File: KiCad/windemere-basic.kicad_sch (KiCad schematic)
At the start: 56 parts, among them J1 Barrel_Jack, J2 Connector, SW1 SW_SPDT, SW2 Push_Button, U1 L7805, U2 74HC00, U3 WD65C02, U4 28C256, U5 62256, U6 WD65C22, U7 MM74C922, U8 HD44780U, U9 MCP102-475, X1 1MHz

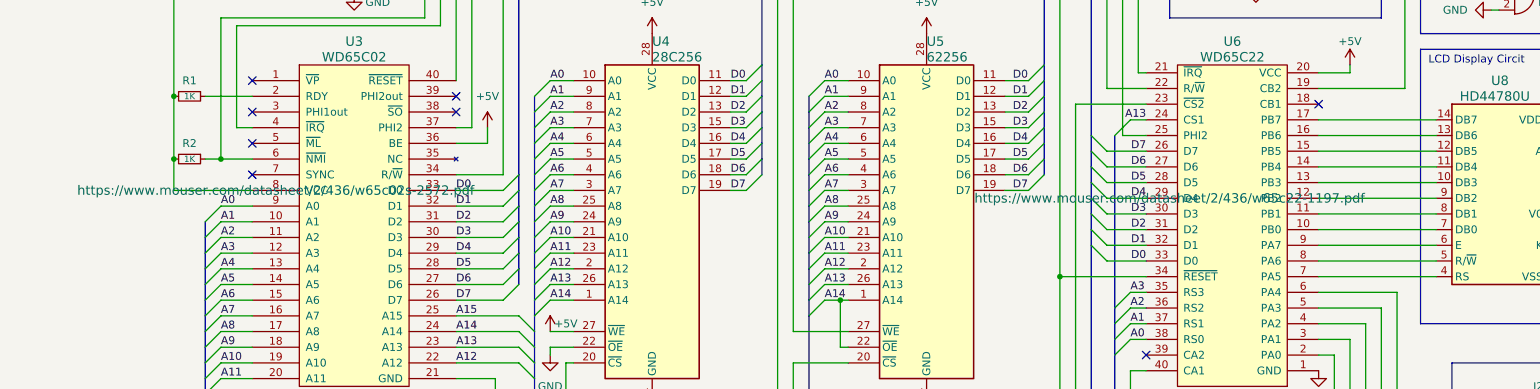
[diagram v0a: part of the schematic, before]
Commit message: Add Zif socket to eprom
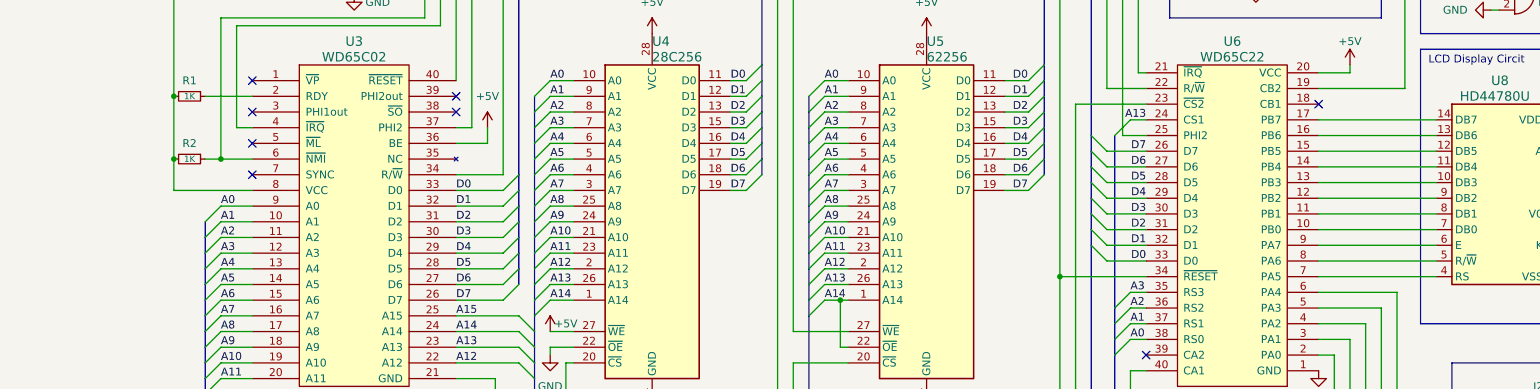
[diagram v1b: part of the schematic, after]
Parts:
- X1: Mouser Part (none) -> 520-TCF100-X
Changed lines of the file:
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@@
     )
     (property "Datasheet" "https://www.mouser.com/datasheet/2/436/w65c02s-2572.pdf" (id 3) (at 34.29 66.04 0)
-      (effects (font (size 1.524 1.524)))
+      (effects (font (size 1.524 1.524)) hide)
     )
     (property "Digikey Part" "~" (id 4) (at 46.99 71.12 0)
@@
       (effects (font (size 1.27 1.27)) hide)
     )
+    (property "Mouser Part" "520-TCF100-X" (id 5) (at 46.99 26.67 0)
+      (effects (font (size 1.27 1.27)) hide)
+    )
     (pin "1")
     (pin "14")
@@
     )
     (property "Datasheet" "https://www.mouser.com/datasheet/2/436/w65c22-1197.pdf" (id 3) (at 179.07 67.31 0)
-      (effects (font (size 1.524 1.524)))
+      (effects (font (size 1.524 1.524)) hide)
     )
     (property "Digikey Part" "~" (id 4) (at 189.23 72.39 0)

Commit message: update socket
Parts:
- SW2: value Push_Button -> Reset Button
- U4: footprint Package_DIP:DIP-28_W15.24mm -> sockets:eeprom_socket
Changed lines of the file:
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@@
       (effects (font (size 1.27 1.27)) (justify right))
     )
-    (property "Value" "Push_Button" (id 1) (at 186.69 31.7499 90)
+    (property "Value" "Reset Button" (id 1) (at 186.69 31.7499 90)
       (effects (font (size 1.27 1.27)) (justify right) hide)
     )
@@
       (effects (font (size 1.524 1.524)) (justify left))
     )
-    (property "Footprint" "Package_DIP:DIP-28_W15.24mm" (id 2) (at 95.25 71.12 0)
+    (property "Footprint" "sockets:eeprom_socket" (id 2) (at 95.25 71.12 0)
       (effects (font (size 1.27 1.27)) hide)
     )
@@
     )
     (path "/cee2649a-819a-40cb-8cce-25f9ff3a4017"
-      (reference "SW2") (unit 1) (value "Push_Button") (footprint "footprints:D6R90F1LFS")
+      (reference "SW2") (unit 1) (value "Reset Button") (footprint "footprints:D6R90F1LFS")
     )
     (path "/af950b64-290c-45ec-af5b-2091c768d43e"
@@
     )
     (path "/d218171f-2b8a-4061-9bea-fd463a7d5174"
-      (reference "U4") (unit 1) (value "28C256") (footprint "Package_DIP:DIP-28_W15.24mm")
+      (reference "U4") (unit 1) (value "28C256") (footprint "sockets:eeprom_socket")
     )
     (path "/40f344b6-38d5-4cfc-82df-1f570acc5b8b"

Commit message: update to current
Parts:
- removed SW1: SW_SPDT, Button_Switch_THT:SW_E-Switch_EG1271_DPDT, symbol Switch:SW_SPDT
- SW2: value Reset Button -> (none); footprint footprints:D6R90F1LFS -> (none)
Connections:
- net at D1.2 (A): now also J1.1
- no-connect marks 10 -> 9
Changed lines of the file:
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@@
   (no_connect (at 30.48 63.5))
   (no_connect (at 30.48 53.34))
-  (no_connect (at 22.86 143.51))
   (no_connect (at 175.26 92.71))
   (no_connect (at 63.5 50.8))
@@
     (stroke (width 0) (type default) (color 0 0 0 0))
   )
-  (wire (pts (xy 22.86 138.43) (xy 19.05 138.43))
-    (stroke (width 0) (type default) (color 0 0 0 0))
-  )
   (bus (pts (xy 226.06 142.24) (xy 226.06 144.78))
     (stroke (width 0) (type default) (color 0 0 0 0))
@@
     (stroke (width 0) (type default) (color 0 0 0 0))
   )
-  (wire (pts (xy 19.05 138.43) (xy 19.05 161.29))
+  (wire (pts (xy 19.05 140.97) (xy 19.05 161.29))
     (stroke (width 0) (type default) (color 0 0 0 0))
   )
@@
     (stroke (width 0) (type default) (color 0 0 0 0))
   )
-  (wire (pts (xy 33.02 140.97) (xy 36.83 140.97))
+  (wire (pts (xy 19.05 140.97) (xy 36.83 140.97))
     (stroke (width 0) (type default) (color 0 0 0 0))
   )
@@
     (effects (font (size 1.27 1.27)) (justify left bottom))
   )
-  (symbol (lib_id "Switch:SW_SPDT") (at 27.94 140.97 0) (mirror y) (unit 1)
-    (in_bom yes) (on_board yes)
-    (property "Reference" "SW1" (id 0) (at 27.94 133.731 0))
-    (property "Value" "SW_SPDT" (id 1) (at 27.94 136.0424 0))
-    (property "Footprint" "Button_Switch_THT:SW_E-Switch_EG1271_DPDT" (id 2) (at 27.94 140.97 0)
-      (effects (font (size 1.27 1.27)) hide)
-    )
-    (property "Datasheet" "~" (id 3) (at 27.94 140.97 0)
-      (effects (font (size 1.27 1.27)) hide)
-    )
-    (pin "1")
-    (pin "2")
-    (pin "3")
-  )
   (symbol (lib_id "power:GND") (at 46.99 34.29 0) (unit 1)
     (in_bom yes) (on_board yes)
@@
       (effects (font (size 1.27 1.27)) hide)
     )
+    (pin "1")
+    (pin "2")
+    (pin "3")
     (pin "4")
     (pin "5")
     (pin "6")
+    (pin "10")
+    (pin "8")
+    (pin "9")
+    (pin "11")
+    (pin "12")
+    (pin "13")
+    (pin "14")
+    (pin "7")
   )
   (symbol (lib_id "power:GND") (at 231.14 36.83 270) (mirror x) (unit 1)
@@
       (effects (font (size 1.27 1.27)) hide)
     )
+    (pin "1")
+    (pin "2")
+    (pin "3")
+    (pin "4")
+    (pin "5")
+    (pin "6")
+    (pin "10")
+    (pin "8")
+    (pin "9")
+    (pin "11")
+    (pin "12")
+    (pin "13")
     (pin "14")
     (pin "7")
@@
       (effects (font (size 1.27 1.27)) hide)
     )
+    (pin "1")
+    (pin "2")
+    (pin "3")
+    (pin "4")
+    (pin "5")
+    (pin "6")
     (pin "10")
     (pin "8")
     (pin "9")
+    (pin "11")
+    (pin "12")
+    (pin "13")
+    (pin "14")
+    (pin "7")
   )
   (symbol (lib_id "Switch:SW_Push_45deg") (at 114.3 171.45 90) (unit 1)
@@
     (pin "2")
     (pin "3")
+    (pin "4")
+    (pin "5")
+    (pin "6")
+    (pin "10")
+    (pin "8")
+    (pin "9")
+    (pin "11")
+    (pin "12")
+    (pin "13")
+    (pin "14")
+    (pin "7")
   )
   (symbol (lib_id "power:GND") (at 231.14 104.14 270) (unit 1)
@@
       (effects (font (size 1.27 1.27)) (justify right))
     )
-    (property "Value" "Reset Button" (id 1) (at 186.69 31.7499 90)
+    (property "Value" "" (id 1) (at 186.69 31.7499 90)
       (effects (font (size 1.27 1.27)) (justify right) hide)
     )
-    (property "Footprint" "footprints:D6R90F1LFS" (id 2) (at 187.96 30.48 0)
+    (property "Footprint" "" (id 2) (at 187.96 30.48 0)
       (effects (font (size 1.27 1.27)) hide)
     )
@@
       (reference "RV1") (unit 1) (value "10K") (footprint "Potentiometer_THT:Potentiometer_Bourns_3296W_Vertical")
     )
-    (path "/0086ff9a-4369-44c7-b877-26a7c9394b1d"
-      (reference "SW1") (unit 1) (value "SW_SPDT") (footprint "Button_Switch_THT:SW_E-Switch_EG1271_DPDT")
-    )
     (path "/cee2649a-819a-40cb-8cce-25f9ff3a4017"
-      (reference "SW2") (unit 1) (value "Reset Button") (footprint "footprints:D6R90F1LFS")
+      (reference "SW2") (unit 1) (value "Reset Button") (footprint "Button_Switch_THT:SW_PUSH_6mm")
     )
     (path "/af950b64-290c-45ec-af5b-2091c768d43e"

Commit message: Update ID's
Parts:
- SW1: renamed from SW2; value (none) -> Reset Button; footprint (none) -> Button_Switch_THT:SW_PUSH_6mm
- renumbered C4 to C1, C3 to C2, C5 to C3, C6 to C4, C1 to C5, C2 to C6, D2 to D1, D1 to D2, J2 to J1, J1 to J2, KB18 to KB10, KB3 to KB11, KB7 to KB12, KB11 to KB13, KB15 to KB14, KB19 to KB15, KB4 to KB16, KB8 to KB17, KB12 to KB18, KB16 to KB19, KB5 to KB2, KB9 to KB3, KB13 to KB4, KB17 to KB5, KB2 to KB6, KB6 to KB7, KB10 to KB8, KB14 to KB9, R8 to R1, R1 to R2, R2 to R3, R3 to R4, R4 to R5, R5 to R6, R6 to R7, R7 to R8, U8 to U1, U3 to U2, U4 to U3, U5 to U4, U6 to U5, U2 to U6, U1 to U8

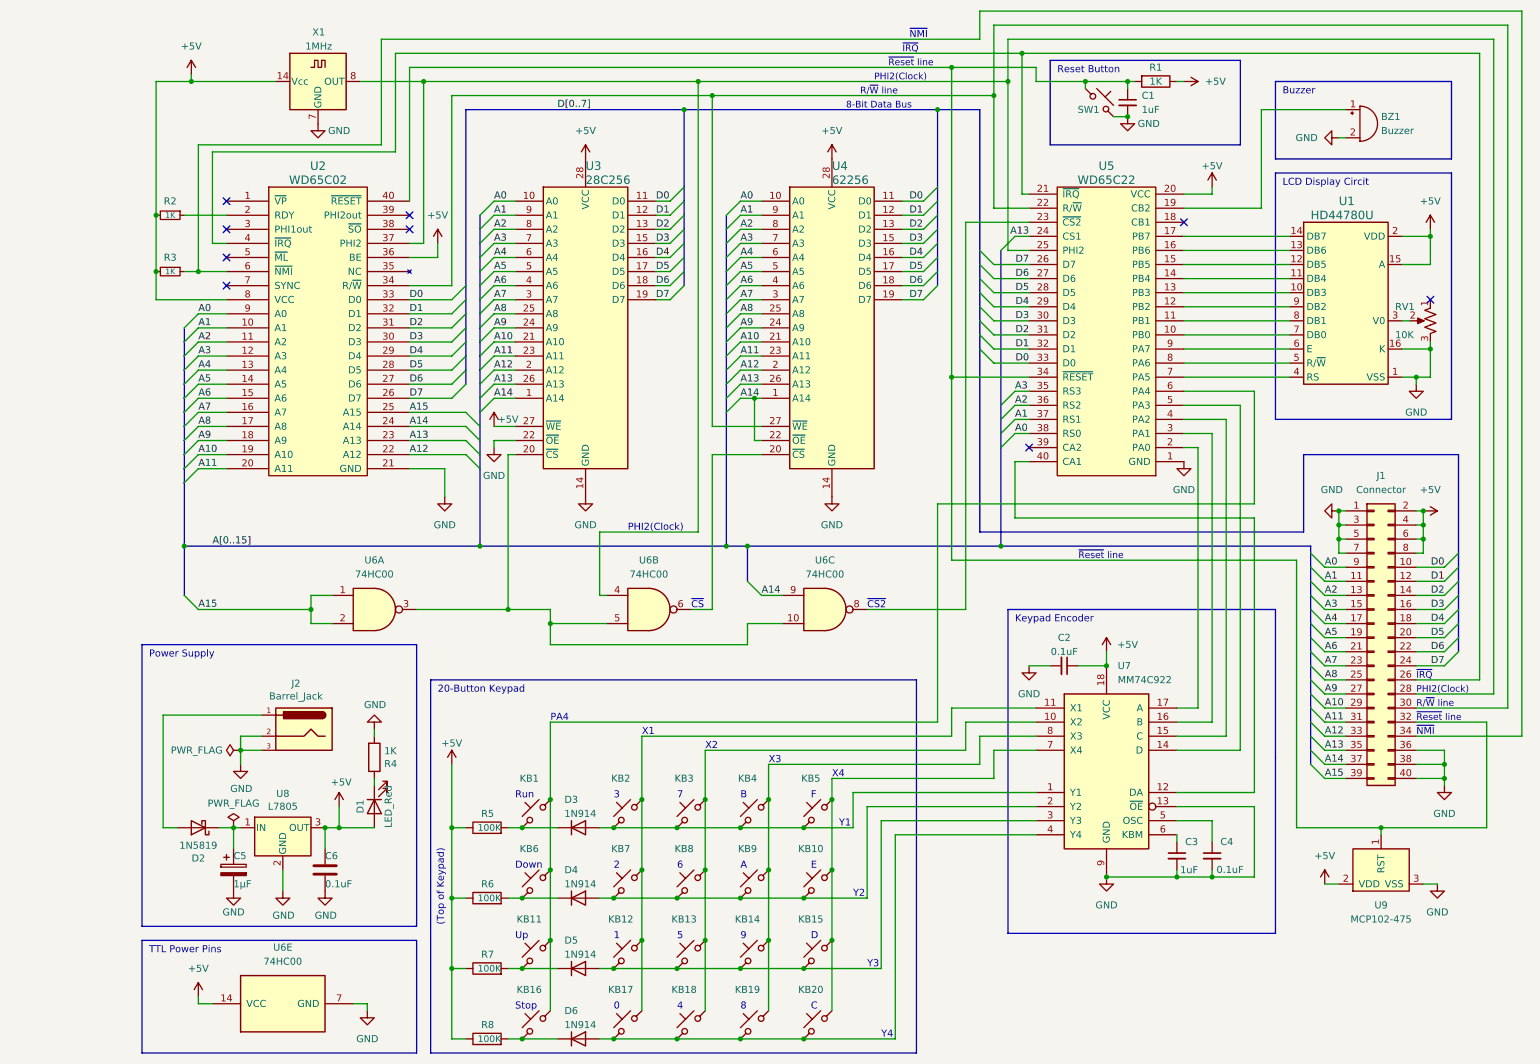
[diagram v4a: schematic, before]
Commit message: Add Bypass caps
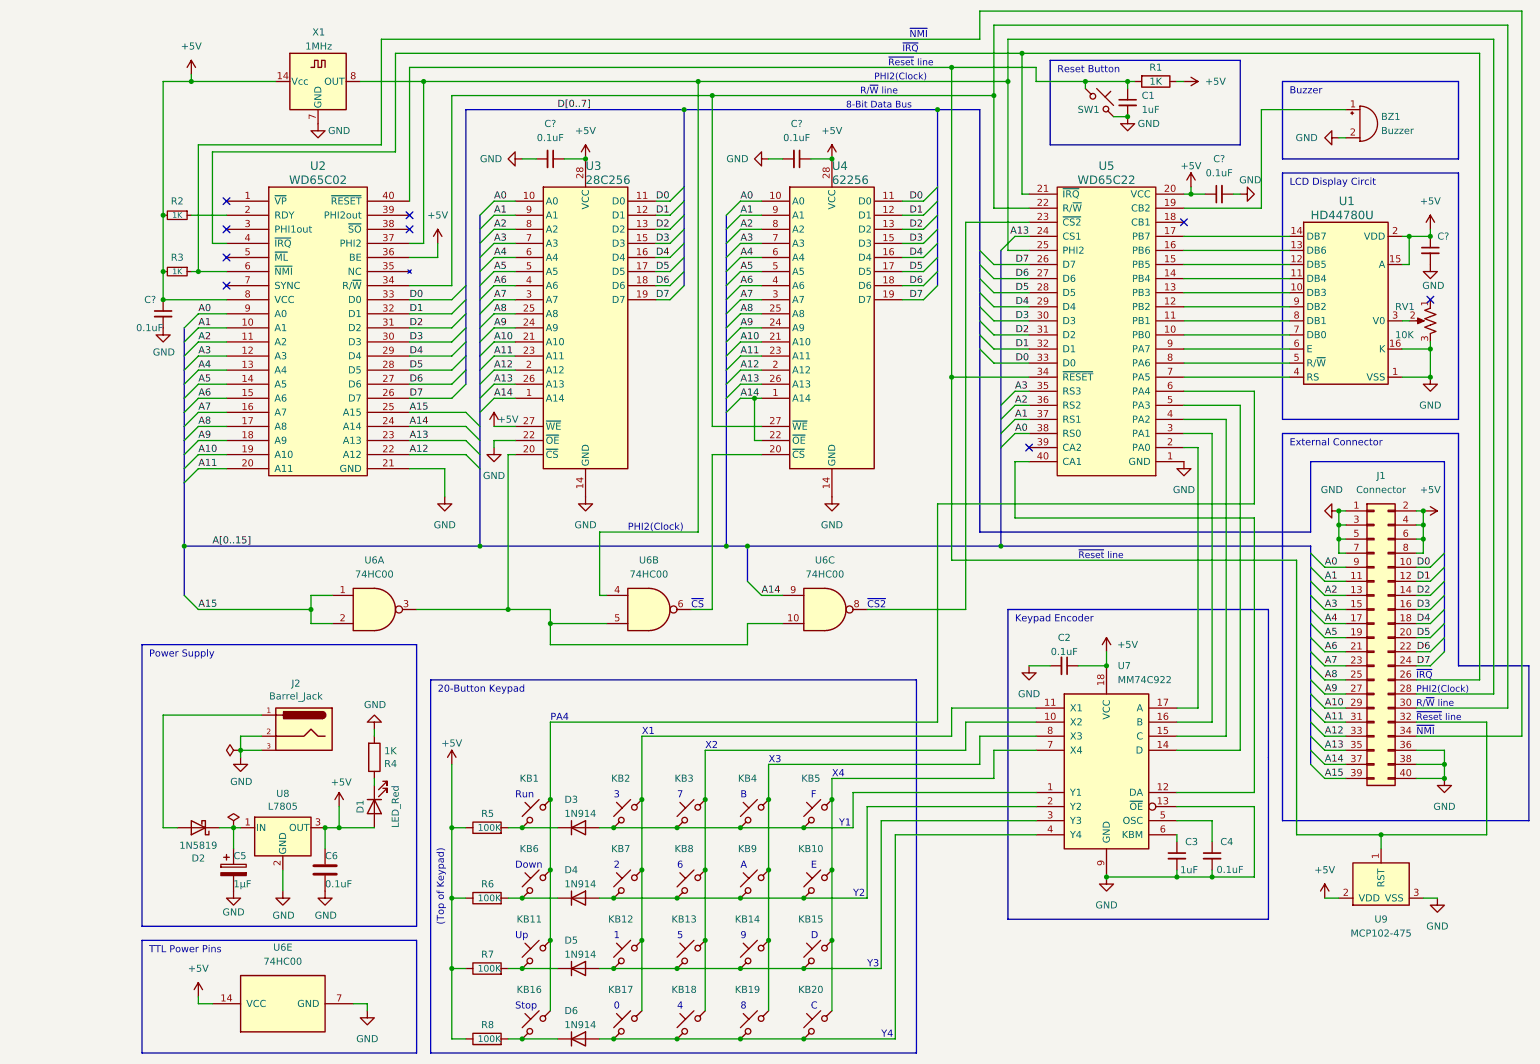
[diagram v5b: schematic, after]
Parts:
- added C? (x4): 0.1uF, Capacitor_THT:C_Disc_D7.0mm_W2.5mm_P5.00mm, symbol Device:C_Small
- added C?: (no value), Capacitor_THT:C_Disc_D7.0mm_W2.5mm_P5.00mm, symbol Device:C_Small
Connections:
- net +5V: now also C?.1, C?.1, C?.1, C?.1, C?.1
- net GND: now also C?.2, C?.2, C?.2, C?.2, C?.2
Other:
- note added: "External Connector"
- moved on the sheet: R2, R3, U9

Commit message: updates
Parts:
- C11: renamed from C?; value (none) -> 0.1uF
- gave numbers to parts that had none: 4
- renumbered C5 to C2, C6 to C3, C2 to C6, C1 to C7, C3 to C8, C4 to C9, D2 to D1, D1 to D2, J2 to J1, J1 to J2, KB8 to KB10, KB13 to KB11, KB18 to KB12, KB4 to KB13, KB9 to KB14, KB14 to KB15, KB19 to KB16, KB5 to KB17, KB10 to KB18, KB15 to KB19, KB6 to KB2, KB11 to KB3, KB16 to KB4, KB2 to KB5, KB7 to KB6, KB12 to KB7, KB17 to KB8, KB3 to KB9, R2 to R1, R3 to R2, R4 to R3, R5 to R4, R6 to R5, R7 to R6, R8 to R7, R1 to R8, U8 to U1, U6 to U2, U2 to U3, U3 to U4, U4 to U5, U5 to U6, U1 to U8
